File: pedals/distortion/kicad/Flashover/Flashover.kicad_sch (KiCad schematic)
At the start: 0 parts

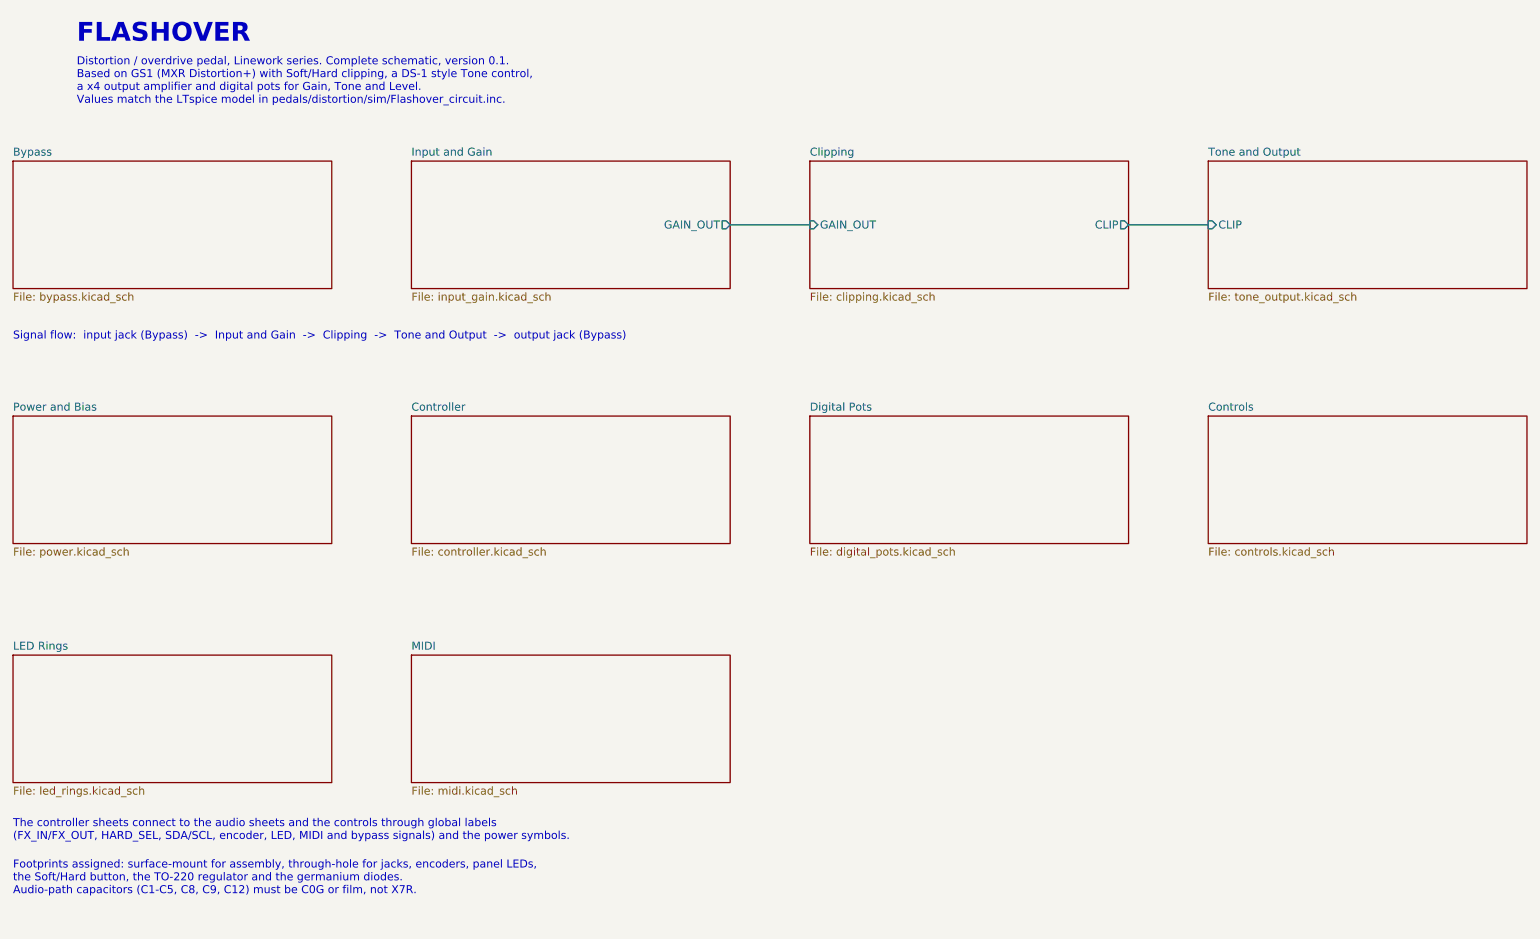
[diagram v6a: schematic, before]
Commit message: Split Flashover into main and control boards; place parts
Main board (Flashover): audio, controller, pots, MIDI, bypass and the five
top-mounted jacks.  Control board (Flashover_Controls): encoders, LED rings,
LED driver, Soft/Hard button and panel LEDs.  J7/J8 2x10 board connector,
M3 mounting holes, regulator laid flat.  Placement only, not yet routed.

Co-Authored-By: Claude Opus 5.5 <noreply@anthropic.com>
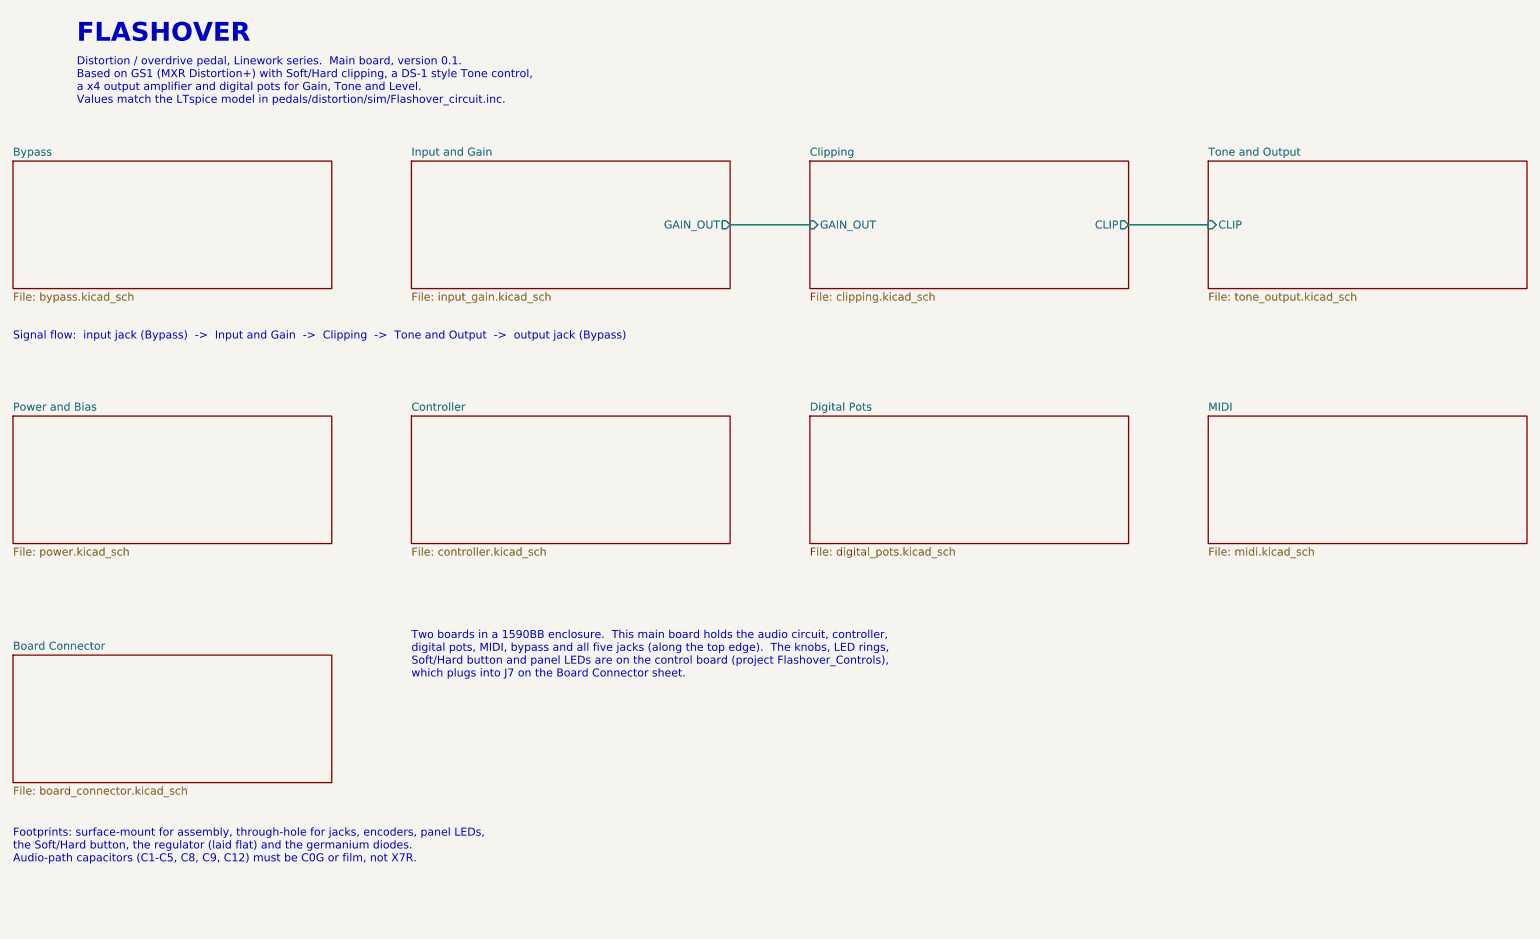
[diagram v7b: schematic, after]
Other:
- removed sheet Controls
- removed sheet LED Rings
- added sheet Board Connector (board_connector.kicad_sch)
- note added: "Distortion / overdrive pedal, Linework series. Main board, version 0.1. Based on GS1 (MXR Distortion+) with Soft/Hard clipping, a DS-1 style Tone control, a x4 output amplifier and digital pots for Gain, Tone and Level. Values match the LTspice model in pedals/distortion/sim/Flashover_circuit.inc."
- note added: "Footprints: surface-mount for assembly, through-hole for jacks, encoders, panel LEDs, the Soft/Hard button, the regulator (laid flat) and the germanium diodes. Audio-path capacitors (C1-C5, C8, C9, C12) must be C0G or film, not X7R."
- note added: "Two boards in a 1590BB enclosure. This main board holds the audio circuit, controller, digital pots, MIDI, bypass and all five jacks (along the top edge). The knobs, LED rings, Soft/Hard button and panel LEDs are on the control board (project Flashover_Controls), which plugs into J7 on the Board Connector sheet."
- note removed: "Distortion / overdrive pedal, Linework series. Complete schematic, version 0.1. Based on GS1 (MXR Distortion+) with Soft/Hard clipping, a DS-1 style Tone control, a x4 output amplifier and digital pots for Gain, Tone and Level. Values match the LTspice model in pedals/distortion/sim/Flashover_circuit.inc."
- note removed: "Footprints assigned: surface-mount for assembly, through-hole for jacks, encoders, panel LEDs, the Soft/Hard button, the TO-220 regulator and the germanium diodes. Audio-path capacitors (C1-C5, C8, C9, C12) must be C0G or film, not X7R."
- note removed: "The controller sheets connect to the audio sheets and the controls through global labels (FX_IN/FX_OUT, HARD_SEL, SDA/SCL, encoder, LED, MIDI and bypass signals) and the power symbols."
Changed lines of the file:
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@@
 		(rev "0.1")
 		(company "GreywireStudio")
-		(comment 1 "Flashover distortion / overdrive - Linework series")
+		(comment 1 "Flashover distortion / overdrive - Linework series - main board")
 	)
 	(wire
@@
 		(effects (font (size 3 3) (bold yes)) (justify left))
 	)
-	(text "Distortion / overdrive pedal, Linework series. Complete schematic, version 0.1.\nBased on GS1 (MXR Distortion+) with Soft/Hard clipping, a DS-1 style Tone control,\na x4 output amplifier and digital pots for Gain, Tone and Level.\nValues match the LTspice model in pedals/distortion/sim/Flashover_circuit.inc."
+	(text "Distortion / overdrive pedal, Linework series.  Main board, version 0.1.\nBased on GS1 (MXR Distortion+) with Soft/Hard clipping, a DS-1 style Tone control,\na x4 output amplifier and digital pots for Gain, Tone and Level.\nValues match the LTspice model in pedals/distortion/sim/Flashover_circuit.inc."
 		(exclude_from_sim no)
 		(at 40.64 45.72 0)
@@
 		(effects (font (size 1.27 1.27)) (justify left))
 	)
-	(text "The controller sheets connect to the audio sheets and the controls through global labels\n(FX_IN/FX_OUT, HARD_SEL, SDA/SCL, encoder, LED, MIDI and bypass signals) and the power symbols."
-		(exclude_from_sim no)
-		(at 30.48 165.1 0)
+	(text "Two boards in a 1590BB enclosure.  This main board holds the audio circuit, controller,\ndigital pots, MIDI, bypass and all five jacks (along the top edge).  The knobs, LED rings,\nSoft/Hard button and panel LEDs are on the control board (project Flashover_Controls),\nwhich plugs into J7 on the Board Connector sheet."
+		(exclude_from_sim no)
+		(at 93.98 137.16 0)
 		(effects (font (size 1.27 1.27)) (justify left))
 	)
-	(text "Footprints assigned: surface-mount for assembly, through-hole for jacks, encoders, panel LEDs,\nthe Soft/Hard button, the TO-220 regulator and the germanium diodes.\nAudio-path capacitors (C1-C5, C8, C9, C12) must be C0G or film, not X7R."
-		(exclude_from_sim no)
-		(at 30.48 172.72 0)
+	(text "Footprints: surface-mount for assembly, through-hole for jacks, encoders, panel LEDs,\nthe Soft/Hard button, the regulator (laid flat) and the germanium diodes.\nAudio-path capacitors (C1-C5, C8, C9, C12) must be C0G or film, not X7R."
+		(exclude_from_sim no)
+		(at 30.48 167.64 0)
 		(effects (font (size 1.27 1.27)) (justify left))
 	)
 	(sheet
-		(at 30.48 99.06)
-		(size 50.8 20.32)
-		(exclude_from_sim no)
-		(in_bom yes)
-		(on_board yes)
-		(dnp no)
-		(fields_autoplaced yes)
-		(stroke
-			(width 0.1524)
-			(type solid)
-		)
-		(fill
-			(color 0 0 0 0.0000)
-		)
-		(property "Sheetname" "Power and Bias"
-			(at 30.48 98.3484 0)
-			(show_name no)
-			(do_not_autoplace no)
-			(effects (font (size 1.27 1.27)) (justify left bottom))
-		)
-		(property "Sheetfile" "power.kicad_sch"
-			(at 30.48 119.9646 0)
-			(show_name no)
-			(do_not_autoplace no)
-			(effects (font (size 1.27 1.27)) (justify left top))
-		)
-		(instances
-			(project "Flashover"
-				(path "/872055d3-e01a-4a82-8c05-28c93674a700"
-					(page "2")
+		(at 30.48 58.42)
+		(size 50.8 20.32)
+		(exclude_from_sim no)
+		(in_bom yes)
+		(on_board yes)
+		(dnp no)
+		(fields_autoplaced yes)
+		(stroke
+			(width 0.1524)
+			(type solid)
+		)
+		(fill
+			(color 0 0 0 0.0000)
+		)
+		(property "Sheetname" "Bypass"
+			(at 30.48 57.7084 0)
+			(show_name no)
+			(do_not_autoplace no)
+			(effects (font (size 1.27 1.27)) (justify left bottom))
+		)
+		(property "Sheetfile" "bypass.kicad_sch"
+			(at 30.48 79.3246 0)
+			(show_name no)
+			(do_not_autoplace no)
+			(effects (font (size 1.27 1.27)) (justify left top))
+		)
+		(instances
+			(project "Flashover"
+				(path "/837bea85-92fd-51b5-9680-1e9b1b02f616"
+					(page "9")
 				)
 			)
@@
 		(instances
 			(project "Flashover"
-				(path "/872055d3-e01a-4a82-8c05-28c93674a700"
+				(path "/837bea85-92fd-51b5-9680-1e9b1b02f616"
 					(page "3")
 				)
@@
 		(instances
 			(project "Flashover"
-				(path "/872055d3-e01a-4a82-8c05-28c93674a700"
+				(path "/837bea85-92fd-51b5-9680-1e9b1b02f616"
 					(page "4")
 				)
@@
 		(instances
 			(project "Flashover"
-				(path "/872055d3-e01a-4a82-8c05-28c93674a700"
+				(path "/837bea85-92fd-51b5-9680-1e9b1b02f616"
 					(page "5")
+				)
+			)
+		)
+	)
+	(sheet
+		(at 30.48 99.06)
+		(size 50.8 20.32)
+		(exclude_from_sim no)
+		(in_bom yes)
+		(on_board yes)
+		(dnp no)
+		(fields_autoplaced yes)
+		(stroke
+			(width 0.1524)
+			(type solid)
+		)
+		(fill
+			(color 0 0 0 0.0000)
+		)
+		(property "Sheetname" "Power and Bias"
+			(at 30.48 98.3484 0)
+			(show_name no)
+			(do_not_autoplace no)
+			(effects (font (size 1.27 1.27)) (justify left bottom))
+		)
+		(property "Sheetfile" "power.kicad_sch"
+			(at 30.48 119.9646 0)
+			(show_name no)
+			(do_not_autoplace no)
+			(effects (font (size 1.27 1.27)) (justify left top))
+		)
+		(instances
+			(project "Flashover"
+				(path "/837bea85-92fd-51b5-9680-1e9b1b02f616"
+					(page "2")
 				)
 			)
@@
 		(instances
 			(project "Flashover"
-				(path "/872055d3-e01a-4a82-8c05-28c93674a700"
+				(path "/837bea85-92fd-51b5-9680-1e9b1b02f616"
 					(page "6")
 				)
@@
 		(instances
 			(project "Flashover"
-				(path "/872055d3-e01a-4a82-8c05-28c93674a700"
+				(path "/837bea85-92fd-51b5-9680-1e9b1b02f616"
 					(page "7")
 				)
@@
 			(color 0 0 0 0.0000)
 		)
-		(property "Sheetname" "Controls"
+		(property "Sheetname" "MIDI"
 			(at 220.98 98.3484 0)
 			(show_name no)
@@
 			(effects (font (size 1.27 1.27)) (justify left bottom))
 		)
-		(property "Sheetfile" "controls.kicad_sch"
+		(property "Sheetfile" "midi.kicad_sch"
 			(at 220.98 119.9646 0)
 			(show_name no)
@@
 		(instances
 			(project "Flashover"
-				(path "/872055d3-e01a-4a82-8c05-28c93674a700"
+				(path "/837bea85-92fd-51b5-9680-1e9b1b02f616"
 					(page "8")
 				)
@@
 			(color 0 0 0 0.0000)
 		)
-		(property "Sheetname" "LED Rings"
+		(property "Sheetname" "Board Connector"
 			(at 30.48 136.4484 0)
 			(show_name no)
@@
 			(effects (font (size 1.27 1.27)) (justify left bottom))
 		)
-		(property "Sheetfile" "led_rings.kicad_sch"
+		(property "Sheetfile" "board_connector.kicad_sch"
 			(at 30.48 158.0646 0)
 			(show_name no)
@@
 		(instances
 			(project "Flashover"
-				(path "/872055d3-e01a-4a82-8c05-28c93674a700"
-					(page "9")
-				)
-			)
-		)
-	)
-	(sheet
-		(at 93.98 137.16)
-		(size 50.8 20.32)
-		(exclude_from_sim no)
-		(in_bom yes)
-		(on_board yes)
-		(dnp no)
-		(fields_autoplaced yes)
-		(stroke
-			(width 0.1524)
-			(type solid)
-		)
-		(fill
-			(color 0 0 0 0.0000)
-		)
-		(property "Sheetname" "MIDI"
-			(at 93.98 136.4484 0)
-			(show_name no)
-			(do_not_autoplace no)
-			(effects (font (size 1.27 1.27)) (justify left bottom))
-		)
-		(property "Sheetfile" "midi.kicad_sch"
-			(at 93.98 158.0646 0)
-			(show_name no)
-			(do_not_autoplace no)
-			(effects (font (size 1.27 1.27)) (justify left top))
-		)
-		(instances
-			(project "Flashover"
-				(path "/872055d3-e01a-4a82-8c05-28c93674a700"
+				(path "/837bea85-92fd-51b5-9680-1e9b1b02f616"
 					(page "10")
 				)
 			)
-		)
-	)
-	(sheet
-		(at 30.48 58.42)
-		(size 50.8 20.32)
-		(exclude_from_sim no)
-		(in_bom yes)
-		(on_board yes)
-		(dnp no)
-		(fields_autoplaced yes)
-		(stroke
-			(width 0.1524)
-			(type solid)
-		)
-		(fill
-			(color 0 0 0 0.0000)
-		)
-		(property "Sheetname" "Bypass"
-			(at 30.48 57.7084 0)
-			(show_name no)
-			(do_not_autoplace no)
-			(effects (font (size 1.27 1.27)) (justify left bottom))
-		)
-		(property "Sheetfile" "bypass.kicad_sch"
-			(at 30.48 79.3246 0)
-			(show_name no)
-			(do_not_autoplace no)
-			(effects (font (size 1.27 1.27)) (justify left top))
-		)
-		(instances
-			(project "Flashover"
-				(path "/872055d3-e01a-4a82-8c05-28c93674a700"
-					(page "11")
-				)
-			)
